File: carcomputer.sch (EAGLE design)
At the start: 73 parts, among them IC1 LM358N, K1 351, Q1 BS170, Q5 TIP136, Q6 BUZ72, Q7 BUZ171, T1 2N2219, T2 2N2219

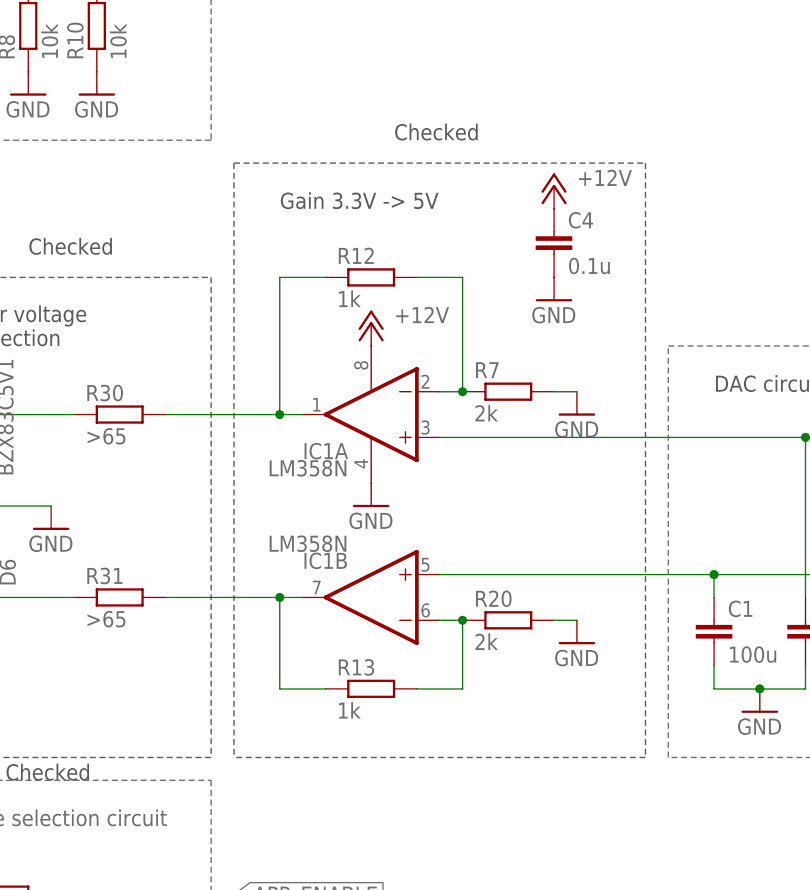
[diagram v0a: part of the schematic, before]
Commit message: Fixed opamp power from battery power to controlled power supply
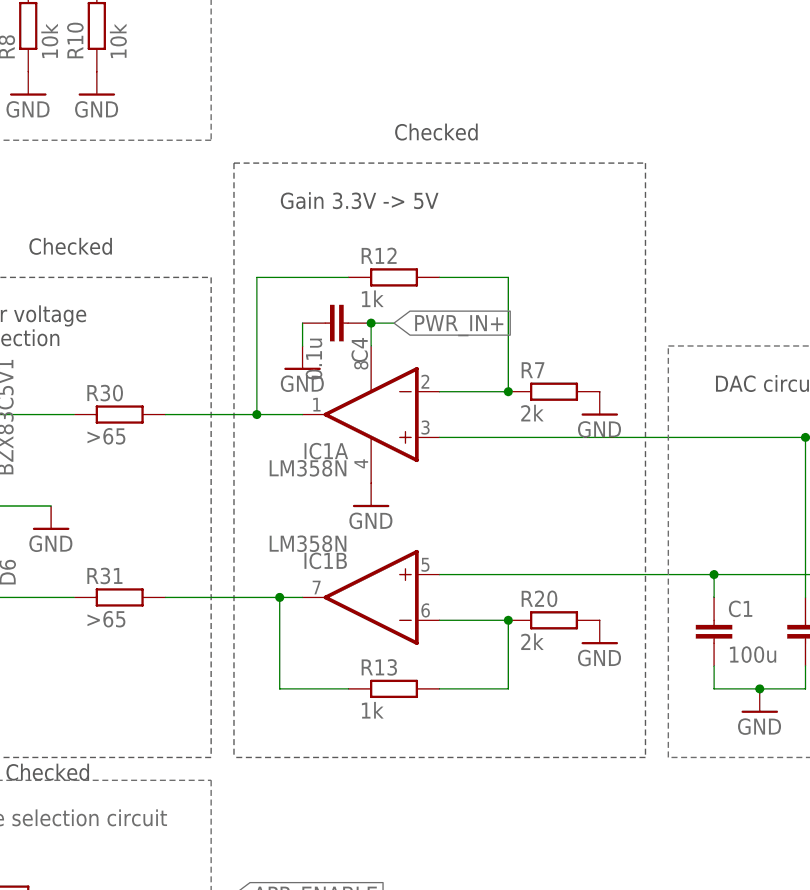
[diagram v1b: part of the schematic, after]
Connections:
- net +12V: no longer C4.1, IC1P.V+
- net PWR_IN+: now also C4.1, IC1P.V+
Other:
- moved on the sheet: C4, R12, R13, R20, R7
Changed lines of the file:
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@@
 <part name="GND33" library="supply1" library_urn="urn:adsk.eagle:library:371" deviceset="GND" device=""/>
 <part name="GND38" library="supply1" library_urn="urn:adsk.eagle:library:371" deviceset="GND" device=""/>
-<part name="P+5" library="supply1" library_urn="urn:adsk.eagle:library:371" deviceset="+12V" device=""/>
 <part name="GND39" library="supply1" library_urn="urn:adsk.eagle:library:371" deviceset="GND" device=""/>
 <part name="D5" library="diode" library_urn="urn:adsk.eagle:library:210" deviceset="BZX85" device="" package3d_urn="urn:adsk.eagle:package:43341/1" value="BZX83C5V1"/>
@@
 <part name="R30" library="rcl" library_urn="urn:adsk.eagle:library:334" deviceset="R-EU_" device="0207/7" package3d_urn="urn:adsk.eagle:package:23493/2" value="&gt;65"/>
 <part name="R31" library="rcl" library_urn="urn:adsk.eagle:library:334" deviceset="R-EU_" device="0207/7" package3d_urn="urn:adsk.eagle:package:23493/2" value="&gt;65"/>
-<part name="P+20" library="supply1" library_urn="urn:adsk.eagle:library:371" deviceset="+12V" device=""/>
 <part name="GND41" library="supply1" library_urn="urn:adsk.eagle:library:371" deviceset="GND" device=""/>
 <part name="C4" library="rcl" library_urn="urn:adsk.eagle:library:334" deviceset="C-EU" device="025-050X050" package3d_urn="urn:adsk.eagle:package:23633/1" value="0.1u"/>
@@
 <attribute name="VALUE" x="218.44" y="91.44" size="1.778" layer="96" rot="MR0"/>
 </instance>
-<instance part="R7" gate="G$1" x="236.22" y="109.22" smashed="yes">
-<attribute name="NAME" x="232.41" y="110.7186" size="1.778" layer="95"/>
-<attribute name="VALUE" x="232.41" y="105.918" size="1.778" layer="96"/>
-</instance>
-<instance part="R12" gate="G$1" x="220.98" y="121.92" smashed="yes">
-<attribute name="NAME" x="217.17" y="123.4186" size="1.778" layer="95"/>
-<attribute name="VALUE" x="217.17" y="118.618" size="1.778" layer="96"/>
-</instance>
-<instance part="R13" gate="G$1" x="220.98" y="76.2" smashed="yes">
-<attribute name="NAME" x="217.17" y="77.6986" size="1.778" layer="95"/>
-<attribute name="VALUE" x="217.17" y="72.898" size="1.778" layer="96"/>
-</instance>
-<instance part="R20" gate="G$1" x="236.22" y="83.82" smashed="yes">
-<attribute name="NAME" x="232.41" y="85.3186" size="1.778" layer="95"/>
-<attribute name="VALUE" x="232.41" y="80.518" size="1.778" layer="96"/>
-</instance>
-<instance part="GND33" gate="1" x="243.84" y="81.28" smashed="yes">
-<attribute name="VALUE" x="241.3" y="78.74" size="1.778" layer="96"/>
-</instance>
-<instance part="GND38" gate="1" x="243.84" y="106.68" smashed="yes">
-<attribute name="VALUE" x="241.3" y="104.14" size="1.778" layer="96"/>
+<instance part="R7" gate="G$1" x="241.3" y="109.22" smashed="yes">
+<attribute name="NAME" x="237.49" y="110.7186" size="1.778" layer="95"/>
+<attribute name="VALUE" x="237.49" y="105.918" size="1.778" layer="96"/>
+</instance>
+<instance part="R12" gate="G$1" x="223.52" y="121.92" smashed="yes">
+<attribute name="NAME" x="219.71" y="123.4186" size="1.778" layer="95"/>
+<attribute name="VALUE" x="219.71" y="118.618" size="1.778" layer="96"/>
+</instance>
+<instance part="R13" gate="G$1" x="223.52" y="76.2" smashed="yes">
+<attribute name="NAME" x="219.71" y="77.6986" size="1.778" layer="95"/>
+<attribute name="VALUE" x="219.71" y="72.898" size="1.778" layer="96"/>
+</instance>
+<instance part="R20" gate="G$1" x="241.3" y="83.82" smashed="yes">
+<attribute name="NAME" x="237.49" y="85.3186" size="1.778" layer="95"/>
+<attribute name="VALUE" x="237.49" y="80.518" size="1.778" layer="96"/>
+</instance>
+<instance part="GND33" gate="1" x="246.38" y="81.28" smashed="yes">
+<attribute name="VALUE" x="243.84" y="78.74" size="1.778" layer="96"/>
+</instance>
+<instance part="GND38" gate="1" x="246.38" y="106.68" smashed="yes">
+<attribute name="VALUE" x="243.84" y="104.14" size="1.778" layer="96"/>
 </instance>
 <instance part="IC1" gate="P" x="220.98" y="106.68" smashed="yes"/>
-<instance part="P+5" gate="1" x="220.98" y="116.84" smashed="yes">
-<attribute name="VALUE" x="223.52" y="116.84" size="1.778" layer="96"/>
-</instance>
 <instance part="GND39" gate="1" x="220.98" y="96.52" smashed="yes">
 <attribute name="VALUE" x="218.44" y="93.98" size="1.778" layer="96"/>
@@
 <attribute name="VALUE" x="189.23" y="83.058" size="1.778" layer="96"/>
 </instance>
-<instance part="P+20" gate="1" x="241.3" y="132.08" smashed="yes">
-<attribute name="VALUE" x="243.84" y="132.08" size="1.778" layer="96"/>
-</instance>
-<instance part="GND41" gate="1" x="241.3" y="119.38" smashed="yes">
-<attribute name="VALUE" x="238.76" y="116.84" size="1.778" layer="96"/>
-</instance>
-<instance part="C4" gate="G$1" x="241.3" y="127" smashed="yes">
-<attribute name="NAME" x="242.824" y="127.381" size="1.778" layer="95"/>
-<attribute name="VALUE" x="242.824" y="122.301" size="1.778" layer="96"/>
+<instance part="GND41" gate="1" x="213.36" y="111.76" smashed="yes">
+<attribute name="VALUE" x="210.82" y="109.22" size="1.778" layer="96"/>
+</instance>
+<instance part="C4" gate="G$1" x="218.44" y="116.84" smashed="yes" rot="R270">
+<attribute name="NAME" x="218.821" y="115.316" size="1.778" layer="95" rot="R270"/>
+<attribute name="VALUE" x="213.741" y="115.316" size="1.778" layer="96" rot="R270"/>
 </instance>
 </instances>
@@
 <segment>
 <pinref part="IC1" gate="A" pin="OUT"/>
-<wire x1="210.82" y1="106.68" x2="213.36" y2="106.68" width="0.1524" layer="91"/>
+<wire x1="208.28" y1="106.68" x2="213.36" y2="106.68" width="0.1524" layer="91"/>
 <pinref part="R12" gate="G$1" pin="1"/>
-<wire x1="215.9" y1="121.92" x2="210.82" y2="121.92" width="0.1524" layer="91"/>
-<wire x1="210.82" y1="121.92" x2="210.82" y2="106.68" width="0.1524" layer="91"/>
+<wire x1="218.44" y1="121.92" x2="208.28" y2="121.92" width="0.1524" layer="91"/>
+<wire x1="208.28" y1="121.92" x2="208.28" y2="106.68" width="0.1524" layer="91"/>
 <pinref part="R30" gate="G$1" pin="2"/>
-<wire x1="198.12" y1="106.68" x2="210.82" y2="106.68" width="0.1524" layer="91"/>
-<junction x="210.82" y="106.68"/>
+<wire x1="198.12" y1="106.68" x2="208.28" y2="106.68" width="0.1524" layer="91"/>
+<junction x="208.28" y="106.68"/>
 </segment>
 </net>
@@
 <pinref part="R7" gate="G$1" pin="2"/>
 <pinref part="GND38" gate="1" pin="GND"/>
-<wire x1="241.3" y1="109.22" x2="243.84" y2="109.22" width="0.1524" layer="91"/>
 </segment>
 <segment>
 <pinref part="R20" gate="G$1" pin="2"/>
 <pinref part="GND33" gate="1" pin="GND"/>
-<wire x1="241.3" y1="83.82" x2="243.84" y2="83.82" width="0.1524" layer="91"/>
 </segment>
 <segment>
@@
 <pinref part="GND41" gate="1" pin="GND"/>
 <pinref part="C4" gate="G$1" pin="2"/>
+<wire x1="213.36" y1="114.3" x2="213.36" y2="116.84" width="0.1524" layer="91"/>
 </segment>
 </net>
@@
 <wire x1="414.02" y1="137.16" x2="414.02" y2="132.08" width="0.1524" layer="91"/>
 </segment>
-<segment>
-<pinref part="IC1" gate="P" pin="V+"/>
-<pinref part="P+5" gate="1" pin="+12V"/>
-</segment>
-<segment>
-<pinref part="P+20" gate="1" pin="+12V"/>
-<pinref part="C4" gate="G$1" pin="1"/>
-</segment>
 </net>
 <net name="PWR_ENABLE" class="0">
@@
 <label x="15.24" y="205.74" size="1.778" layer="95" rot="R180" xref="yes"/>
 </segment>
+<segment>
+<pinref part="IC1" gate="P" pin="V+"/>
+<wire x1="220.98" y1="114.3" x2="220.98" y2="116.84" width="0.1524" layer="91"/>
+<pinref part="C4" gate="G$1" pin="1"/>
+<wire x1="220.98" y1="116.84" x2="223.52" y2="116.84" width="0.1524" layer="91"/>
+<junction x="220.98" y="116.84"/>
+<label x="223.52" y="116.84" size="1.778" layer="95" xref="yes"/>
+</segment>
 </net>
 <net name="N$11" class="0">
@@
 <pinref part="R12" gate="G$1" pin="2"/>
 <pinref part="R7" gate="G$1" pin="1"/>
-<wire x1="226.06" y1="121.92" x2="231.14" y2="121.92" width="0.1524" layer="91"/>
-<wire x1="231.14" y1="121.92" x2="231.14" y2="109.22" width="0.1524" layer="91"/>
+<wire x1="228.6" y1="121.92" x2="236.22" y2="121.92" width="0.1524" layer="91"/>
+<wire x1="236.22" y1="121.92" x2="236.22" y2="109.22" width="0.1524" layer="91"/>
 <pinref part="IC1" gate="A" pin="-IN"/>
-<wire x1="228.6" y1="109.22" x2="231.14" y2="109.22" width="0.1524" layer="91"/>
-<junction x="231.14" y="109.22"/>
+<wire x1="228.6" y1="109.22" x2="236.22" y2="109.22" width="0.1524" layer="91"/>
+<junction x="236.22" y="109.22"/>
 </segment>
 </net>
@@
 <pinref part="IC1" gate="B" pin="-IN"/>
 <pinref part="R20" gate="G$1" pin="1"/>
-<wire x1="228.6" y1="83.82" x2="231.14" y2="83.82" width="0.1524" layer="91"/>
+<wire x1="228.6" y1="83.82" x2="236.22" y2="83.82" width="0.1524" layer="91"/>
 <pinref part="R13" gate="G$1" pin="2"/>
-<wire x1="231.14" y1="83.82" x2="231.14" y2="76.2" width="0.1524" layer="91"/>
-<wire x1="231.14" y1="76.2" x2="226.06" y2="76.2" width="0.1524" layer="91"/>
-<junction x="231.14" y="83.82"/>
+<wire x1="236.22" y1="83.82" x2="236.22" y2="76.2" width="0.1524" layer="91"/>
+<wire x1="236.22" y1="76.2" x2="228.6" y2="76.2" width="0.1524" layer="91"/>
+<junction x="236.22" y="83.82"/>
 </segment>
 </net>
@@
 <wire x1="210.82" y1="86.36" x2="213.36" y2="86.36" width="0.1524" layer="91"/>
 <wire x1="210.82" y1="86.36" x2="210.82" y2="76.2" width="0.1524" layer="91"/>
-<wire x1="210.82" y1="76.2" x2="215.9" y2="76.2" width="0.1524" layer="91"/>
+<wire x1="210.82" y1="76.2" x2="218.44" y2="76.2" width="0.1524" layer="91"/>
 <pinref part="R31" gate="G$1" pin="2"/>
 <wire x1="198.12" y1="86.36" x2="210.82" y2="86.36" width="0.1524" layer="91"/>

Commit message: Implemented circuits for claxon and engine cutoff
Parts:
- added CLAXON_CONN, ENGINE_CUTOFF_CONN: (no value), con-ptr500:AK300/2
- added D7, D8: 1N4148DO35-7, diode:1N4148DO35-7
- added K2, K3: RT184012, relay:RT184012
- added R32, R33: 2k, rcl:R-EU_0207/7
- added T3, T4: BC618, transistor-npn:BC618
- T1, T2: value 2N2219 -> BC618; device transistor:2N2219 -> transistor-npn:BC618
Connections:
- new net CLAXON_ENABLE: R33.2, U$1.IO25
- new net ENGINE_CUTOFF_DISABLE: R32.2, U$1.IO26
- new net N$19: ENGINE_CUTOFF_CONN-1.KL, K32.P
- new net N$20: ENGINE_CUTOFF_CONN-2.KL, K32.S
- new net N$22: D7.A, K31.1, T3.C
- new net N$23: D8.A, K21.1, T4.C
- new net N$25: R33.1, T4.B
- new net N$26: R32.1, T3.B
- new net N$27: CLAXON_CONN-1.KL, K22.P
- new net N$28: CLAXON_CONN-2.KL, K22.S
- net +12V: now also D7.C, D8.C, K21.2, K31.2
- net GND: now also T3.E, T4.E
- net IO25: no longer U$1.IO25
- net IO26: no longer U$1.IO26
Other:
- note added: "CLAXON CIRCUIT"
- note added: "ENGINE CUTOFF CIRCUIT"
- note added: "Manual override"
- note added: "Steering wheel claxon"

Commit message: unknown changes
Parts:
- removed C3: 100u, rcl:C-EU025-050X050
- removed JP_IO25, JP_IO26: (no value), pinhead:PINHD-1X3
- removed Q6: BUZ72, transistor-fet:BUZ72
- removed Q7: BUZ171, transistor-fet:BUZ171
- removed R24: 150, rcl:R-EU_0207/7
- removed R25: 500?, rcl:R-EU_0207/7
- removed R26: 1k, rcl:R-EU_0207/7
- removed R27: 10k, rcl:R-EU_0207/7
- removed R28: 2k, rcl:R-EU_0207/7
- APP, CLAXON_CONN, ECU, ENGINE_CUTOFF_CONN: device con-ptr500:AK300/2 -> con-ptr500-custom:AK300/2
- U$2: value MCP2515_DEVBOARD -> MCP2515_DEVBOARDINVERTED; device MCP2515:MCP2515_DEVBOARD -> MCP2515:MCP2515_DEVBOARDINVERTED
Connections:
- removed net IN: Q6.G, R28.2
- removed net IO25: JP_IO25.2
- removed net IO26: JP_IO26.2
- removed net N$21: C3.1, R24.2, R25.2
- removed net N$24: Q7.G, R26.2, R27.1
- removed net OUT: Q7.D, R24.1
- net +5V: no longer JP_IO25.3, JP_IO26.3, Q7.S, R27.2
- net GND: no longer C3.2, JP_IO25.1, JP_IO26.1, Q6.D, Q6.S, R25.1, R26.1, R28.1
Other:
- note removed: "- +14V"
- note removed: "3.3V PWM 80 kHz"
- note removed: "5V PWM"
- note removed: "???"
- note removed: "DAC"
- note removed: "EXAMPLES"
- note removed: "Load"

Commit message: Routed almost first complete single board
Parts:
- added X1, X2: 2.52B-ZR, con-jst-custom:2.52B-ZR
- D1, D7, D8: value 1N4148DO35-7 -> 1N40047; device diode:1N4148DO35-7 -> diode-custom:1N40047
- D2, D3: value 1N4004 -> 1N40047; device diode:1N4004 -> diode-custom:1N40047
- D4, D5, D6: device diode:BZX85 -> diode-custom:BZX857
- DISPLAY: value B4B-ZR -> 2.54B-ZR; device con-jst-custom:B4B-ZR -> con-jst-custom:2.54B-ZR
- OBDII: value B2B-ZR -> 2.52B-ZR; device con-jst-custom:B2B-ZR -> con-jst-custom:2.52B-ZR
- PWR, STEERING_WHEEL: value B3B-ZR -> 2.53B-ZR; device con-jst-custom:B3B-ZR -> con-jst-custom:2.53B-ZR
- R1, R11, R14, R2, R21, R32, R33, R9: device rcl:R-EU_0207/7 -> rcl:R-EU_0309/10
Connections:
- net +12V: now also PWR-1.1; no longer D7.C, D8.C, JP_PWR_12V.2, K21.2, K31.2, PWR-3.1
- net +3V3: now also DISPLAY-1.1; no longer DISPLAY-4.1
- net +5V: now also K11.1; no longer K11.2
- net APP_0_IN: now also X1-2.1
- net APP_1_IN: now also X1-1.1
- net BTN_0: now also R4.2, STEERING_WHEEL-1.1; no longer R5.2, STEERING_WHEEL-3.1
- net BTN_1: now also R5.2, STEERING_WHEEL-3.1; no longer R4.2, STEERING_WHEEL-1.1
- net GND: now also DISPLAY-4.1; no longer DISPLAY-1.1
- net GPS_RX: now also JP_UART2.3; no longer JP_UART2.2
- net GPS_TX: now also JP_UART2.2; no longer JP_UART2.3
- net I2C1_SCL: now also DISPLAY-2.1; no longer DISPLAY-3.1
- net I2C1_SDA: now also DISPLAY-3.1; no longer DISPLAY-2.1
- net IGNITION: now also PWR-3.1; no longer PWR-1.1
- net N$1: now also K11.2; no longer K11.1
- net N$6: now also K13.P, X2-2.1; no longer K12.P
- net N$7: now also K12.P, X2-1.1; no longer K13.P
- net PWR_IN+: now also D7.C, D8.C, JP_PWR_12V.2, K21.2, K31.2
- net UART0_RX: now also JP_UART0.3; no longer JP_UART0.2
- net UART0_TX: now also JP_UART0.2; no longer JP_UART0.3
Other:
- moved on the sheet: DISPLAY-1, DISPLAY-2, DISPLAY-3, DISPLAY-4, ECU-1, ECU-2, K1, PWR-1, PWR-2, PWR-3
